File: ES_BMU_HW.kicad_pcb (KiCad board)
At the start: 2 copper layers, 80 x 60 mm, 96 parts, among them IC1 ADBMS6821CCSZ, J1 Conn_02x02_Top_Bottom, J2 Conn_02x02_Top_Bottom, J3 Conn_02x03_Top_Bottom, J4 Conn_02x06_Top_Bottom, J5 Conn_02x03_Top_Bottom, J6 Conn_02x04_Top_Bottom, Q1 SQ2362CES, Q3 SQ2362CES, Q6 SQ2362CES, Q7 SQ2362CES, SW1 SW_Nidec_CAS-120A1, SW3 SW_Nidec_CAS-120A1, T1 74941301, U1 TPS542025, U15 SN65HVD234, U2 LM393, U3 STM32G474CBTx, U4 SN65HVD234, U5 ADS1113IDGS, U7 TLV777

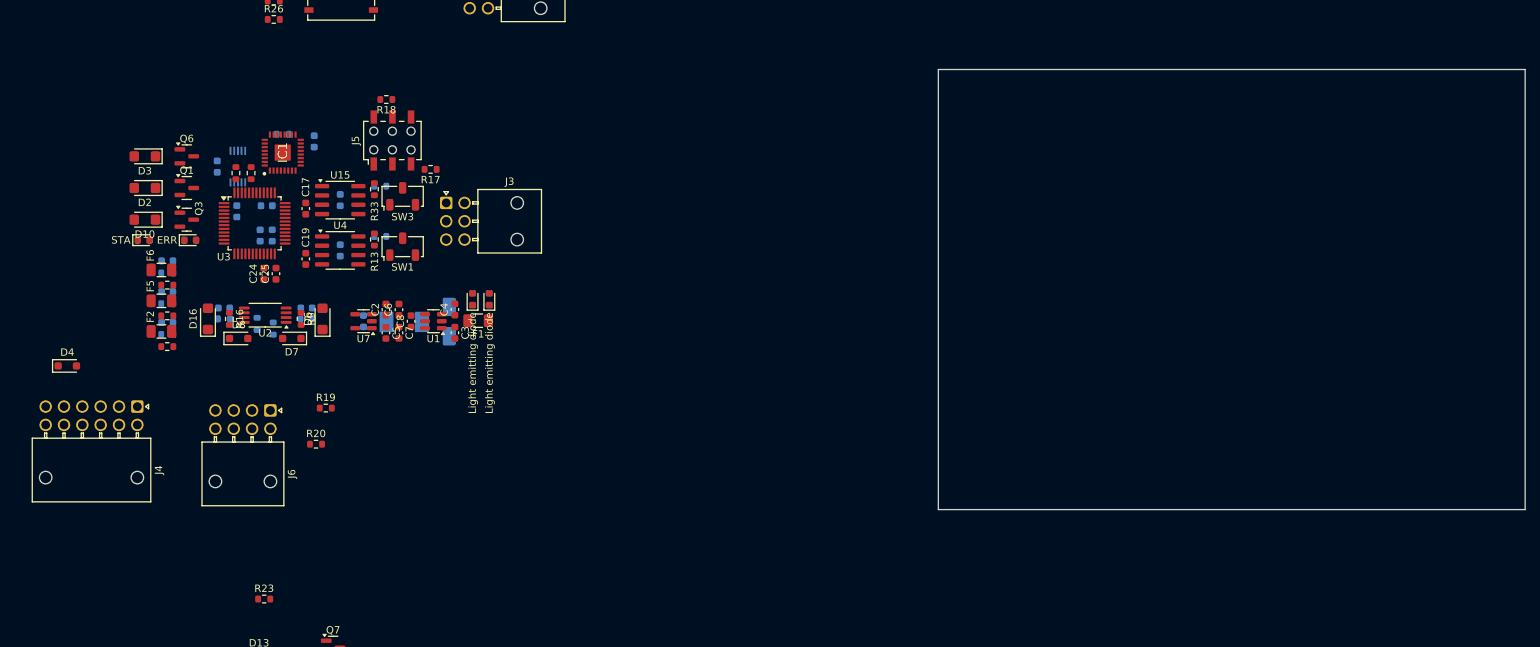
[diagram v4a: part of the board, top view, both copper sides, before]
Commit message: Fusibles eliminats de la mesura dels contactors auxiliars Canvi de lloc dels enables del CAN Emplaçament dels inputs, CAN i LEDs al Layout
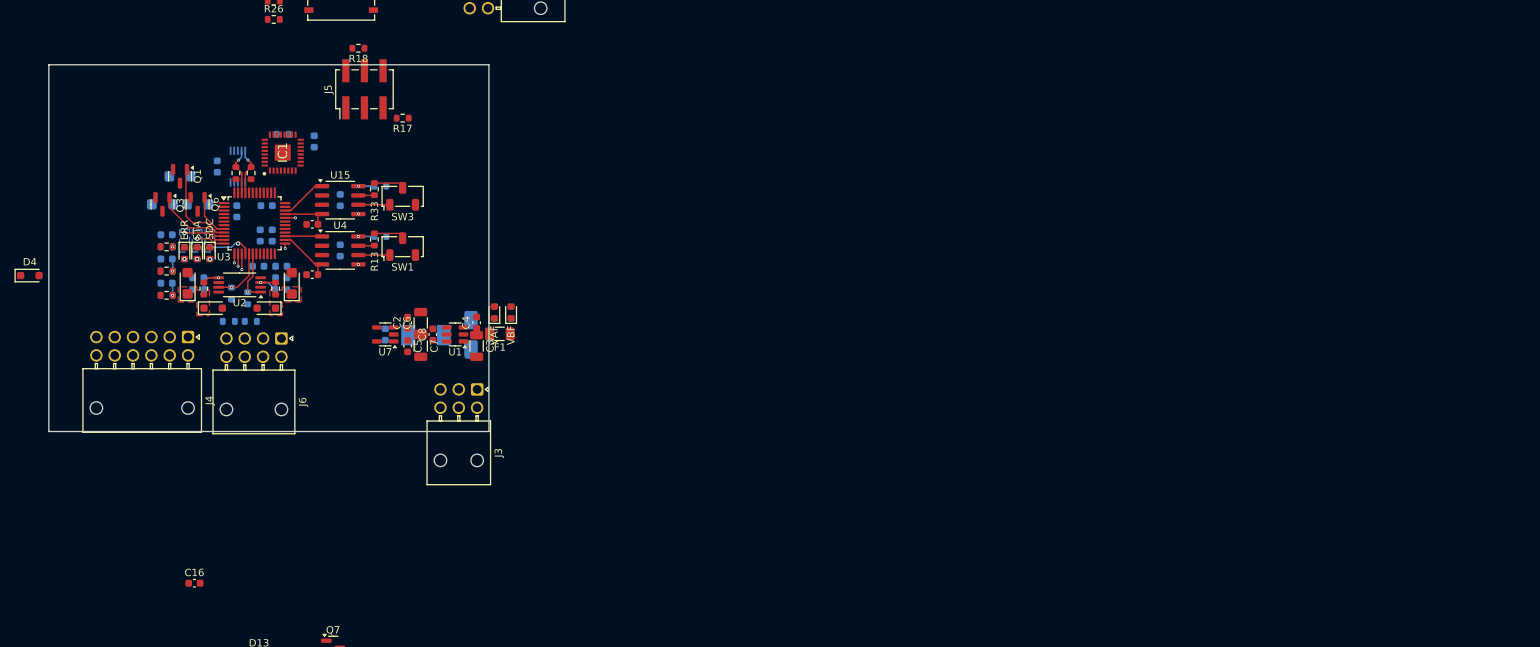
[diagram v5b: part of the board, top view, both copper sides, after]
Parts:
- removed F2, F5, F6: Fuse, Fuse:Fuse_1206_3216Metric
- removed R23: 100k, Resistor_SMD:R_0603_1608Metric
- added C16: 100n, Capacitor_SMD:C_0603_1608Metric, F.Cu at (105.6, 138.5)
- added D5: LED, LED_SMD:LED_0603_1608Metric, F.Cu at (107.7, 93.5)
- added R10: 100, Resistor_SMD:R_0603_1608Metric, B.Cu at (107.7, 93.5)
- C24, C25, D10, D2, D3, R19, R20: moved to B.Cu
- C3, C6, C7: footprint Capacitor_SMD:C_0603_1608Metric -> Capacitor_SMD:C_1206_3216Metric
- J5: footprint Connector_Wuerth:Wuerth_WR-PHD_610006243021_SMD_2x03_P2.54mm_Vertical -> Connector_PinHeader_2.54mm:PinHeader_2x03_P2.54mm_Vertical_SMD
- moved J3 25.8 mm to (144.1, 112.0), turned to -90 degrees
- moved R20 20.5 mm to (110.3, 102.8)
- moved R19 15.6 mm to (113.3, 102.8)
- moved D4 13.3 mm to (83.2, 96.5)
- moved J4 11.7 mm to (104.7, 104.9)
- moved J6 9.93 mm to (117.5, 105.1)
- moved D3 9.73 mm to (106.0, 86.8), turned to 0 degrees
- moved J5 7.96 mm to (128.8, 71.1)
- moved R18 7.96 mm to (128.0, 65.5)
- moved R17 7.96 mm to (134.0, 75.1)
- moved D14 7.50 mm to (106.0, 93.5), turned to -90 degrees
- moved R22 7.50 mm to (106.0, 93.5), turned to -90 degrees
- moved R1 6.99 mm to (101.8, 99.2)
- moved Q6 6.72 mm to (106.0, 86.8), turned to -90 degrees
- moved D6 6.41 mm to (118.9, 97.6)
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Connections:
- J6 pad 7: SDCendState -> ActiveButtonState
- J6 pad 8: ActiveButtonState -> SDCendState
- R1 pad 2: Net-(F2-Pad1) -> RawAuxAIRpre
- R5 pad 2: Net-(F5-Pad1) -> RawAuxAIR-
- R7 pad 2: Net-(F6-Pad1) -> RawAuxAIR+
- U3 pad 16: unconnected-(U3-PB0-Pad16) -> LEDSDCstate
- U3 pad 2: /stm32/FDCAN1_EN -> unconnected-(U3-PC13-Pad2)
- U3 pad 25: unconnected-(U3-PB11-Pad25) -> /stm32/FDCAN2_EN
- U3 pad 3: /stm32/FDCAN2_EN -> unconnected-(U3-PC14-Pad3)
- U3 pad 32: unconnected-(U3-PA10-Pad32) -> /stm32/FDCAN1_EN
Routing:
- net AuxAIRpre: track 0.00 -> 14.7 mm, vias 0 -> 2
- net AuxAIR-: track 0.00 -> 12.6 mm, vias 0 -> 2
- net ControlAIR-: track 0.00 -> 12.5 mm
- net /stm32/FDCAN2_EN: track 0.00 -> 11.6 mm, vias 0 -> 2
- net AuxAIR+: track 0.00 -> 10.6 mm, vias 0 -> 2
- net ControlAIRpre: track 0.00 -> 10.4 mm
- net /stm32/FDCAN1_EN: track 0.00 -> 10.2 mm, vias 0 -> 2
- net /stm32/FDCAN2_RX: track 0.00 -> 8.44 mm
- net SDCendState: track 0.00 -> 7.79 mm, vias 0 -> 1
- net ActiveButtonState: track 0.00 -> 7.28 mm, vias 0 -> 1
- net /stm32/FDCAN1_RX: track 0.00 -> 7.13 mm
- net /stm32/FDCAN1_TX: track 0.00 -> 6.41 mm
- net /stm32/I2C2_SCL: track 0.00 -> 6.38 mm, vias 0 -> 1
- net /stm32/I2C2_SDA: track 0.00 -> 6.38 mm, vias 0 -> 1
- net LEDSDCstate: track 0.00 -> 6.10 mm, vias 0 -> 1
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- added copper zone on B.Cu, net LEDBMSerror
- added copper zone on B.Cu, net LEDBMSstate
- added copper zone on B.Cu, net LEDSDCstate
- added copper zone on F.Cu, net Net-(D16-A1)
- added copper zone on F.Cu, net Net-(D6-A1)
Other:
- board size 80 x 60 mm -> 60 x 50 mm
- copper layers 2 -> 4

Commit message: Layout avançat amb el placement acabat
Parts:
- removed R27, R28: 10k, Resistor_SMD:R_0603_1608Metric
- added H1: MountingHole_Pad, MountingHole:MountingHole_3.5mm, F.Cu at (142.0, 116.0)
- added H2: MountingHole_Pad, MountingHole:MountingHole_3.5mm, F.Cu at (102.0, 116.0)
- added H3: MountingHole_Pad, MountingHole:MountingHole_3.5mm, F.Cu at (102.0, 76.0)
- added H4: MountingHole_Pad, MountingHole:MountingHole_3.5mm, F.Cu at (143.0, 86.2)
- C17, C19, C28, C7, D13, R13, R17, R18, R33: moved to B.Cu
- J5: footprint Connector_PinHeader_2.54mm:PinHeader_2x03_P2.54mm_Vertical_SMD -> Connector_PinHeader_1.27mm:PinHeader_2x03_P1.27mm_Vertical_SMD
- U5: moved to F.Cu
- moved Q7 50.6 mm to (102.4, 101.8), turned to 180 degrees
- moved D13 48.3 mm to (102.9, 101.8)
- moved J2 45.1 mm to (133.9, 101.7)
- moved C16 36.7 mm to (105.2, 101.8), turned to -90 degrees
- moved D15 26.4 mm to (122.4, 102.0), turned to 0 degrees
- moved R29 26.4 mm to (122.4, 102.0), turned to 0 degrees
- moved J1 26.1 mm to (133.8, 74.0)
- moved D4 25.8 mm to (105.7, 109.0), turned to 90 degrees
- moved C28 25.6 mm to (119.2, 77.0), turned to -90 degrees
- moved D17 24.2 mm to (122.4, 103.7), turned to 0 degrees
- moved R30 24.2 mm to (122.4, 103.7), turned to 0 degrees
- moved J3 22.4 mm to (133.9, 92.1), turned to 0 degrees
- moved F1 20.2 mm to (127.0, 104.8)
- moved R18 19.8 mm to (115.5, 80.9)
- moved C4 18.1 mm to (126.2, 100.4), turned to 180 degrees
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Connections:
- J1 pad 1: isoIPA -> unconnected-(J1-Pin_1-Pad1)
- J1 pad 3: isoIMA -> isoIPA
- J1 pad 4: unconnected-(J1-Pin_4-Pad4) -> isoIMA
- J2 pad 1: unconnected-(J2-Pin_1-Pad1) -> GND
- J2 pad 4: GND -> unconnected-(J2-Pin_4-Pad4)
- J4 pad 1: SDC -> AIR+Coil-
- J4 pad 10: RawAuxAIR+ -> PwrAuxAIR
- J4 pad 11: RawAuxAIR- -> PwrAuxAIR
- J4 pad 12: RawAuxAIRpre -> PwrAuxAIR
- J4 pad 2: SDC -> AIR-Coil-
- J4 pad 3: SDC -> AIRpreCoil-
- J4 pad 4: PwrAuxAIR -> RawAuxAIRpre
- J4 pad 5: PwrAuxAIR -> RawAuxAIR-
- J4 pad 6: PwrAuxAIR -> RawAuxAIR+
- J4 pad 7: AIR+Coil- -> SDC
- J4 pad 8: AIR-Coil- -> SDC
- J4 pad 9: AIRpreCoil- -> SDC
- J6 pad 4: BMSerror -> BMSerrorOutput
- J6 pad 7: ActiveButtonState -> ActiveButton
- J6 pad 8: SDCendState -> SDCinput
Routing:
- net +3.3V: track 0.00 -> 46.5 mm, vias 0 -> 7
- net HallVout: track 0.00 -> 45.0 mm, vias 0 -> 1
- net AIR-Coil-: track 0.00 -> 32.6 mm, vias 0 -> 1
- net AIR+Coil-: track 0.00 -> 28.4 mm, vias 0 -> 1
- net AIRpreCoil-: track 0.00 -> 28.3 mm, vias 0 -> 1
- net BMSerrorOutput: track 0.00 -> 27.4 mm, vias 0 -> 1
- net RawAuxAIR+: track 0.00 -> 23.0 mm
- net GND: track 0.00 -> 22.5 mm, vias 0 -> 6
- net BMSerror: track 0.00 -> 21.9 mm, vias 0 -> 2
- net SDCinput: track 0.00 -> 21.5 mm, vias 0 -> 1
- net RawAuxAIR-: track 0.00 -> 21.5 mm
- net +24V: track 0.00 -> 21.1 mm, vias 0 -> 3
- net RawAuxAIRpre: track 0.00 -> 20.0 mm
- net ActiveButton: track 0.00 -> 18.6 mm, vias 0 -> 1
- net +5V: track 0.00 -> 17.1 mm, vias 0 -> 1
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- added copper zone on F.Cu, net +24V
- added copper zone on B.Cu, net +3.3V
- added copper zone on B.Cu, net +5V
- added copper zone on F.Cu, net +5V
- added copper zone on B.Cu, net GND
- added copper zone on F.Cu, net GND
- added copper zone on F.Cu, net VBAT
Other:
- board size 60 x 50 mm -> 50 x 50 mm

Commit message: Plans de coure actualitzats Separació per creepage i clearance corregit
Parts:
- added REF**: Symbol_HighVoltage_NoTriangle_2x5mm_Copper, Symbol:Symbol_HighVoltage_NoTriangle_2x5mm_Copper, F.Cu at (134.4, 81.1)
- moved C18 0.57 mm to (117.7, 75.5)
- renumbered SW3 to CAN1, SW1 to CAN2
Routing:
- net +3.3V: track 46.5 -> 43.5 mm, vias 7 -> 9
- net Net-(IC1-RTO): track 0.00 -> 2.86 mm, vias 0 -> 1
- net GND: vias 6 -> 8
- added copper zone on F.Cu, net +3.3V
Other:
- board text added: "BMU v1.0"
- board text added: "LV"
- board text added: "OFF"
- board text added: "ON"
- board text added: "TS"

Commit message: Layout acabat amb components, pistes i serigrafia completa
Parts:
- added G***: LOGO, silkscreen:eussms18w, F.Cu at (112.2, 105.3)
- IC1: footprint EUSSMS:QFN50P500X500X80-33N-D -> Package_CSP:LFCSP-32-1EP_5x5mm_P0.5mm_EP3.1x3.1mm
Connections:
- J4 pad 7: SDC -> SDCinput
- J4 pad 8: SDC -> SDCinput
- J4 pad 9: SDC -> SDCinput
- R2 pad 1: /GPIO/3.3V -> +3.3V
- R24 pad 1: /GPIO/3.3V -> +3.3V
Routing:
- net +3.3V: track 43.5 -> 83.8 mm, vias 9 -> 14
- net GND: track 22.5 -> 44.1 mm, vias 8 -> 24
- net +5V: track 17.1 -> 33.9 mm, vias 1 -> 2
- net /stm32/SPI1_WAKE: track 8.82 -> 13.7 mm
- net Net-(CAN2-B): track 0.00 -> 3.74 mm, vias 0 -> 1
- net AuxAIR+: track 12.2 -> 10.5 mm
- net Net-(U15-Rs): track 0.00 -> 1.43 mm, vias 0 -> 1
- net AuxAIR-: track 12.6 -> 12.0 mm
- net Net-(U1-FB): vias 0 -> 1
- net Net-(D17-A): vias 0 -> 1
- added copper zone on B.Cu, net SDCinput
- added copper zone on F.Cu, net SDCinput
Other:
- outline, holes or cut-outs redrawn
- board text added: "EUSS MOTORSPORT 44/26 Martí Xuclà"
